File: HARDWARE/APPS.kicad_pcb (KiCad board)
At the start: 2 copper layers, 100 x 75 mm, 69 parts, among them J4 Sygnały, J5 Diagnostyka, J8 Zasilanie+CAN, K1 FINDER-30.22, Q1 BSS138, SW1 SW_Push, U1 STM32L4P5RET6, U3 LM1117-3.3, U4 LM1117-3.3, U5 LM1117-3.3, U6 MCP2562-H-SN, U7 MCP6001-OT, U8 MCP6001-OT, Y1 Crystal_GND24

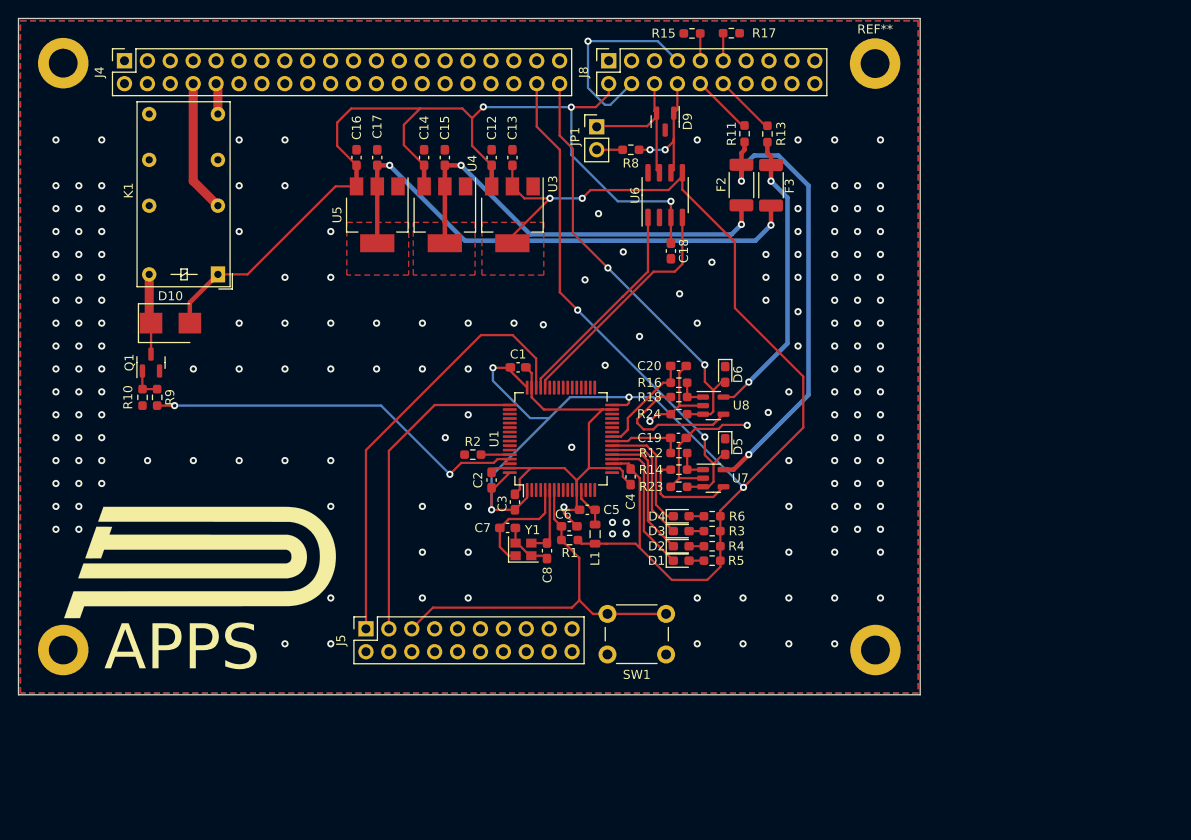
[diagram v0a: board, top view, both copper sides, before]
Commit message: Align components on the PCB
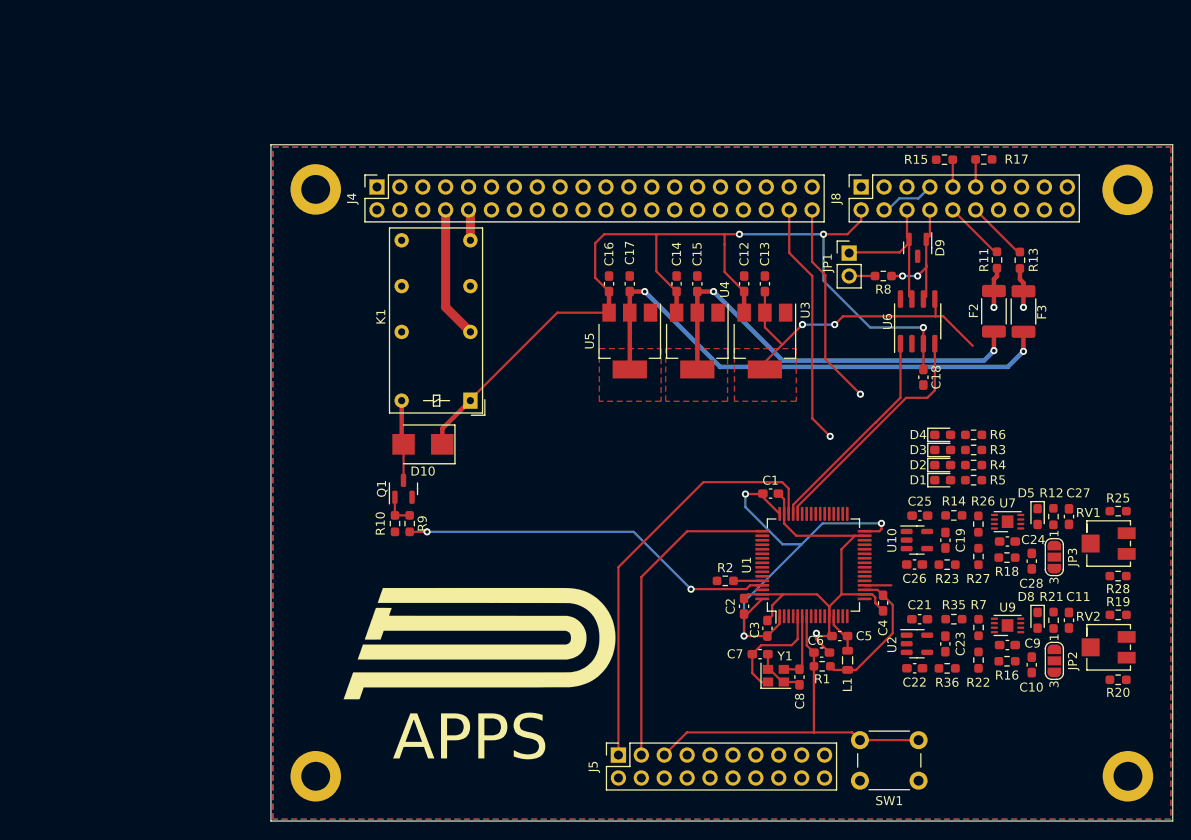
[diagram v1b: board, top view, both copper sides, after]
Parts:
- removed C20: 100n, Capacitor_SMD:C_0603_1608Metric_Pad1.08x0.95mm_HandSolder
- removed D6: D_TVS, Diode_SMD:D_0603_1608Metric_Pad1.05x0.95mm_HandSolder
- removed R24: 100k, Resistor_SMD:R_0603_1608Metric_Pad0.98x0.95mm_HandSolder
- removed U8: MCP6001-OT, Package_TO_SOT_SMD:SOT-23-5
- added C10: 10n, Capacitor_SMD:C_0603_1608Metric_Pad1.08x0.95mm_HandSolder, F.Cu at (184.4, 124.3)
- added C11: 10n, Capacitor_SMD:C_0603_1608Metric_Pad1.08x0.95mm_HandSolder, F.Cu at (188.5, 119.3)
- added C21: 100n, Capacitor_SMD:C_0603_1608Metric_Pad1.08x0.95mm_HandSolder, F.Cu at (172.0, 119.2)
- added C22: 100n, Capacitor_SMD:C_0603_1608Metric_Pad1.08x0.95mm_HandSolder, F.Cu at (171.4, 124.6)
- added C23: 100n, Capacitor_SMD:C_0603_1608Metric_Pad1.08x0.95mm_HandSolder, F.Cu at (174.8, 121.9)
- added C24: 100n, Capacitor_SMD:C_0603_1608Metric_Pad1.08x0.95mm_HandSolder, F.Cu at (181.7, 110.6)
- added C25: 100n, Capacitor_SMD:C_0603_1608Metric_Pad1.08x0.95mm_HandSolder, F.Cu at (172.0, 107.7)
- added C26: 100n, Capacitor_SMD:C_0603_1608Metric_Pad1.08x0.95mm_HandSolder, F.Cu at (171.4, 113.1)
- added C27: 10n, Capacitor_SMD:C_0603_1608Metric_Pad1.08x0.95mm_HandSolder, F.Cu at (188.5, 107.8)
- added C28: 10n, Capacitor_SMD:C_0603_1608Metric_Pad1.08x0.95mm_HandSolder, F.Cu at (184.4, 112.8)
- added C9: 100n, Capacitor_SMD:C_0603_1608Metric_Pad1.08x0.95mm_HandSolder, F.Cu at (181.7, 122.1)
- added D8: D_TVS, Diode_SMD:D_0603_1608Metric_Pad1.05x0.95mm_HandSolder, F.Cu at (185.1, 119.3)
- added JP2: POT/DAC, Jumper:SolderJumper-3_P1.3mm_Open_RoundedPad1.0x1.5mm_NumberLabels, F.Cu at (186.9, 123.8)
- added JP3: POT/DAC, Jumper:SolderJumper-3_P1.3mm_Open_RoundedPad1.0x1.5mm_NumberLabels, F.Cu at (186.9, 112.3)
- added R19: 10k, Resistor_SMD:R_0603_1608Metric_Pad0.98x0.95mm_HandSolder, F.Cu at (194.0, 118.7)
- added R20: 33k, Resistor_SMD:R_0603_1608Metric_Pad0.98x0.95mm_HandSolder, F.Cu at (194.0, 125.9)
- added R21: 100k, Resistor_SMD:R_0603_1608Metric_Pad0.98x0.95mm_HandSolder, F.Cu at (186.8, 119.3)
- added R22: TBD, Resistor_SMD:R_0603_1608Metric_Pad0.98x0.95mm_HandSolder, F.Cu at (178.5, 123.7)
- added R25: 10k, Resistor_SMD:R_0603_1608Metric_Pad0.98x0.95mm_HandSolder, F.Cu at (194.0, 107.2)
- added R26: TBD, Resistor_SMD:R_0603_1608Metric_Pad0.98x0.95mm_HandSolder, F.Cu at (178.5, 108.6)
- added R27: TBD, Resistor_SMD:R_0603_1608Metric_Pad0.98x0.95mm_HandSolder, F.Cu at (178.5, 112.2)
- added R28: 33k, Resistor_SMD:R_0603_1608Metric_Pad0.98x0.95mm_HandSolder, F.Cu at (194.0, 114.4)
- added R35: 4k7, Resistor_SMD:R_0603_1608Metric_Pad0.98x0.95mm_HandSolder, F.Cu at (175.8, 119.2)
- added R36: 4k7, Resistor_SMD:R_0603_1608Metric_Pad0.98x0.95mm_HandSolder, F.Cu at (175.0, 124.6)
- added R7: TBD, Resistor_SMD:R_0603_1608Metric_Pad0.98x0.95mm_HandSolder, F.Cu at (178.5, 120.1)
- added RV1: 1k, Potentiometer_SMD:Potentiometer_Bourns_3214J_Horizontal, F.Cu at (192.9, 110.8)
- added RV2: 1k, Potentiometer_SMD:Potentiometer_Bourns_3214J_Horizontal, F.Cu at (192.9, 122.3)
- added U10: MCP6001, Package_TO_SOT_SMD:SOT-23-5, F.Cu at (171.7, 110.4)
- added U2: MCP6001, Package_TO_SOT_SMD:SOT-23-5, F.Cu at (171.7, 121.9)
- added U9: MCP6N11-005, Package_DFN_QFN:TDFN-8-1EP_3x2mm_P0.5mm_EP1.3x1.4mm, F.Cu at (181.7, 119.9)
- R12: value 4k7 -> 100k
- R14: value 0R -> 4k7
- R16: value 4k7 -> 0R
- R23: value 100k -> 4k7
- U7: value MCP6001-OT -> MCP6N11-005; footprint Package_TO_SOT_SMD:SOT-23-5 -> Package_DFN_QFN:TDFN-8-1EP_3x2mm_P0.5mm_EP1.3x1.4mm
- moved R16 47.7 mm to (181.7, 123.9)
- moved R12 42.1 mm to (186.8, 107.8), turned to 90 degrees
- moved R18 40.5 mm to (181.7, 112.4), turned to 0 degrees
- moved D5 35.5 mm to (185.1, 107.8)
- moved U7 33.0 mm to (181.7, 108.4), turned to 180 degrees
- moved G*** 32.3 mm to (122.3, 121.6)
- moved C19 31.7 mm to (174.8, 110.4), turned to -90 degrees
- moved C13 31.3 mm to (154.8, 82.0)
- moved C16 31.3 mm to (137.5, 82.0)
- moved U3 31.3 mm to (154.8, 88.3)
- moved J5 31.3 mm to (138.6, 134.3)
- moved ? 31.3 mm to (195.0, 71.6)
- moved ? 31.3 mm to (195.1, 136.6)
- moved ? 31.3 mm to (105.0, 136.6)
- moved C1 31.3 mm to (155.5, 105.3)
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- renumbered REF** to ?
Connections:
- net /CAN-RX renamed /CAN_RX
- net /CAN-TX renamed /CAN_TX
- net /PowerModule/VO_POT1 renamed /Power Module/VO_POT1
- net /PowerModule/VO_POT2 renamed /Power Module/VO_POT2
- C19 pad 1: /SENSOR1 -> Net-(C19-Pad1)
- C19 pad 2: GND -> /SENSOR2
- D10 pad 1: Net-(D10-Pad1) -> +5V
- D10 pad 2: +5V -> Net-(D10-A)
- D5 pad 2: SIG_APPS1 -> SIG_APPS2
- K1 pad A2: Net-(D10-Pad1) -> Net-(D10-A)
- Q1 pad 3: Net-(D10-Pad1) -> Net-(D10-A)
- R12 pad 1: /SENSOR1 -> SIG_APPS2
- R12 pad 2: Net-(R12-Pad2) -> GND
- R14 pad 1: Net-(R12-Pad2) -> Net-(R14-Pad1)
- R14 pad 2: Net-(R14-Pad2) -> Net-(C19-Pad1)
- R16 pad 1: /SENSOR2 -> Net-(U9-EN)
- R16 pad 2: Net-(R16-Pad2) -> 3V3_POT1
- R18 pad 1: Net-(R16-Pad2) -> Net-(U7-EN)
- R18 pad 2: Net-(R18-Pad2) -> 3V3_POT2
- R23 pad 1: SIG_APPS1 -> Net-(C19-Pad1)
- R23 pad 2: GND -> Net-(U10-+)
- U1 pad 20: /LED1 -> /DAC_REF1
- U1 pad 21: /LED2 -> /DAC_REF2
- U1 pad 22: /LED3 -> unconnected-(U1-PA6-Pad22)
- U1 pad 23: /LED4 -> unconnected-(U1-PA7-Pad23)
- U1 pad 26: unconnected-(U1-Pad26) -> /LED1
- U1 pad 27: unconnected-(U1-Pad27) -> /LED2
- U1 pad 28: unconnected-(U1-Pad28) -> /LED3
- U1 pad 29: unconnected-(U1-Pad29) -> /LED4
- U7 pad 1: Net-(R12-Pad2) -> Net-(U7-FG)
- U7 pad 2: GND -> Net-(JP3-C)
- U7 pad 3: SIG_APPS1 -> SIG_APPS2
- U7 pad 4: Net-(R14-Pad2) -> GND
- U7 pad 5: 3V3_POT1 -> GND
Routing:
- net /3V3_SYS: track 179.9 -> 101.9 mm, vias 6 -> 5
- net 3V3_POT1: track 51.4 -> 4.44 mm, vias 2 -> 1
- net GND: track 106.3 -> 62.3 mm, vias 182 -> 1
- net SIG_APPS1: track 57.2 -> 27.0 mm, vias 2 -> 1
- net 3V3_POT2: track 32.8 -> 4.47 mm, vias 2 -> 1
- net SIG_APPS2: track 48.1 -> 22.7 mm, vias 2 -> 1
- net /LED1: track 15.8 -> 0.00 mm
- net Net-(R18-Pad2): track 15.7 -> 0.00 mm
- net /LED2: track 14.9 -> 0.00 mm
- net /LED3: track 13.9 -> 0.00 mm
- net /LED4: track 13.3 -> 0.00 mm
- net /SENSOR2: track 11.6 -> 0.00 mm
- net Net-(R14-Pad2): track 11.3 -> 0.00 mm
- net Net-(D10-Pad1): track 8.93 -> 0.00 mm
- net Net-(D10-A): track 0.00 -> 8.93 mm
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
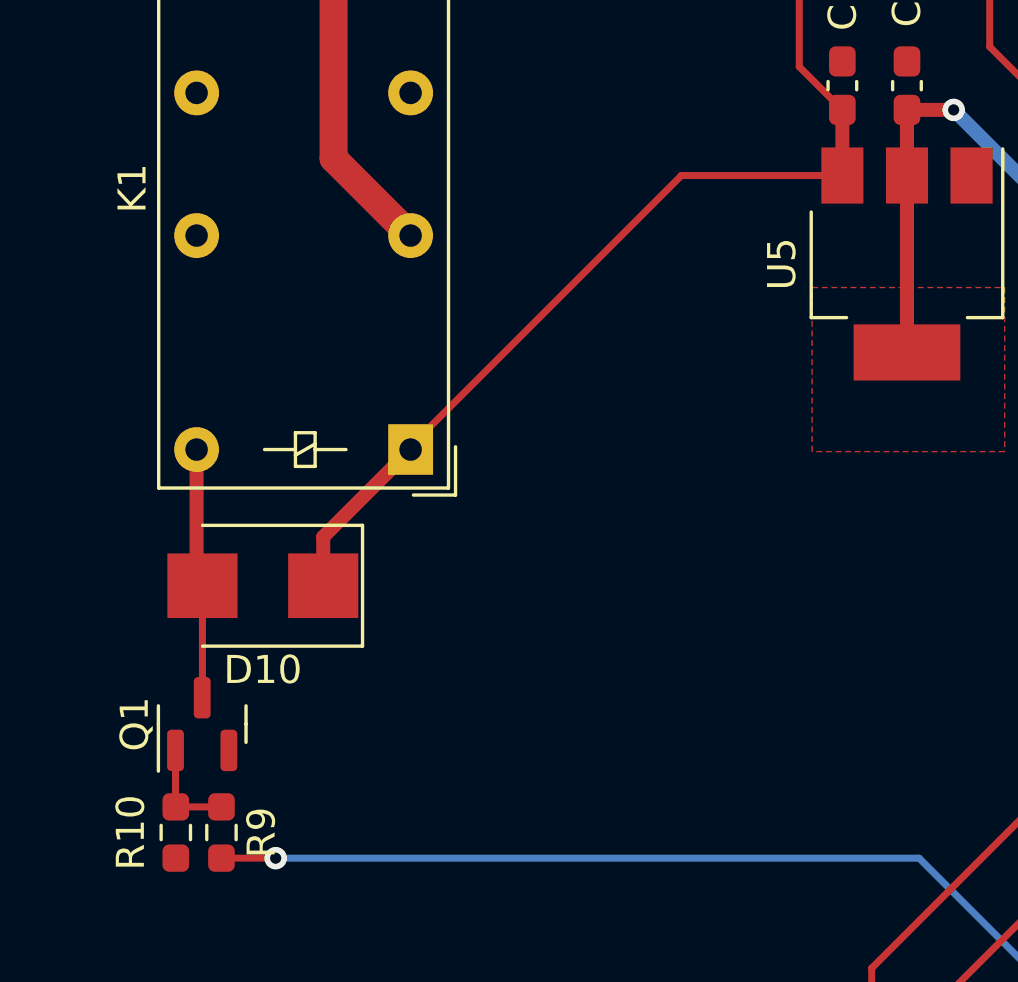
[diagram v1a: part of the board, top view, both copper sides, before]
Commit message: KiCad project refactor
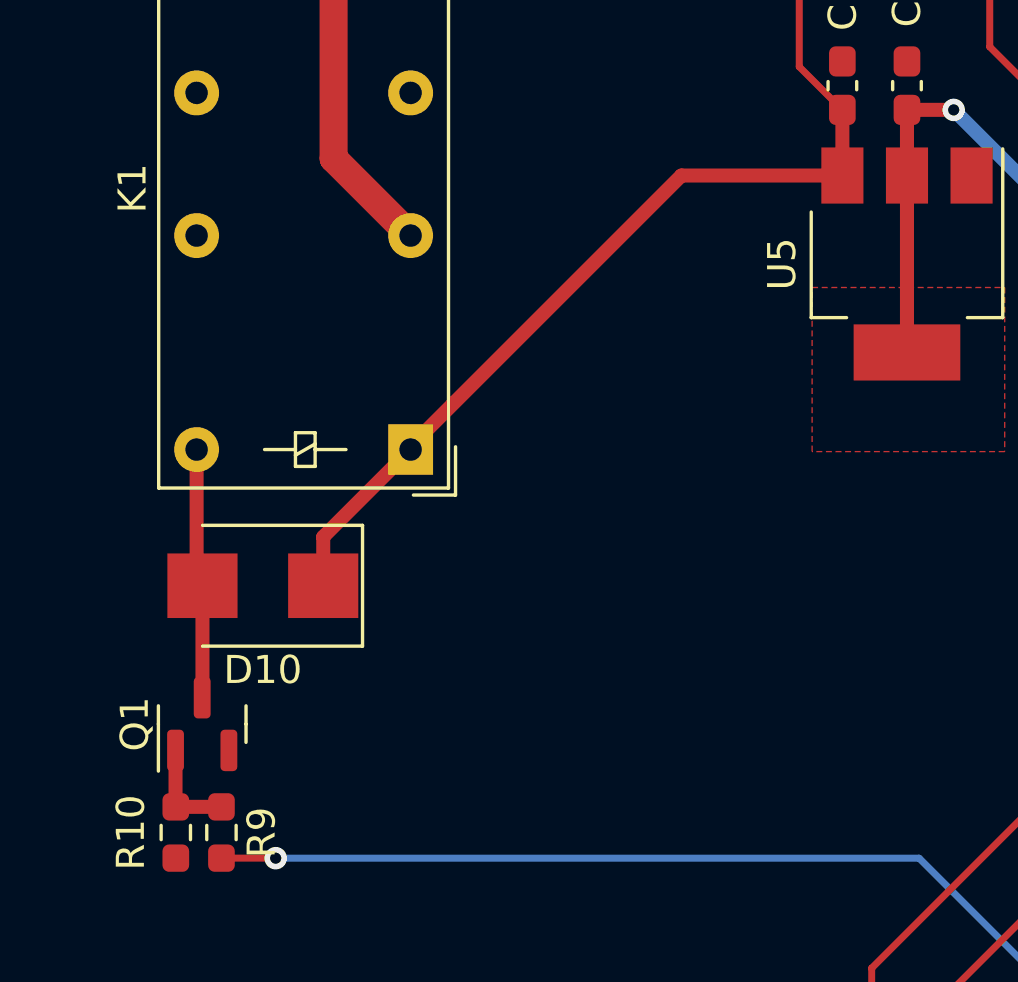
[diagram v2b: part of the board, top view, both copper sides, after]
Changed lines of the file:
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@@
     (effects (font (size 5 5) (thickness 1)))
-  )
-  (dimension (type aligned) (layer "Dwgs.User")
-    (pts (xy 72.046008 52.573201) (xy 172.046008 52.573201))
-    (height -8.373201)
-    (gr_text "100.0000 mm" (at 122.046008 43.05) (layer "Dwgs.User")
-      (effects (font (size 1 1) (thickness 0.15)))
-    )
-    (format (prefix "") (suffix "") (units 3) (units_format 1) (precision 4))
-    (style (thickness 0.1) (arrow_length 1.27) (text_position_mode 0) (extension_height 0.58642) (extension_offset 0.5) keep_text_aligned)
   )
   (segment (start 167.065 116.779994) (end 166.722006 116.437) (width 0.25) (layer "F.Cu") (net 1))
@@
   (segment (start 172.399 86.846907) (end 172.399 88.6364) (width 0.25) (layer "F.Cu") (net 5))
   (segment (start 136 77.5008) (end 136 81.3221) (width 0.25) (layer "F.Cu") (net 5))
-  (segment (start 122.1615 94.8385) (end 131.8042 85.1958) (width 0.25) (layer "F.Cu") (net 5))
+  (segment (start 122.1615 94.8385) (end 131.8042 85.1958) (width 0.5) (layer "F.Cu") (net 5))
   (segment (start 161.32 76.5) (end 163.9756 76.5) (width 0.25) (layer "F.Cu") (net 5))
   (segment (start 150.3518 77.627) (end 150.3518 80.6879) (width 0.25) (layer "F.Cu") (net 5))
-  (segment (start 131.8042 85.1958) (end 137.5362 85.1958) (width 0.25) (layer "F.Cu") (net 5))
+  (segment (start 131.8042 85.1958) (end 137.5362 85.1958) (width 0.5) (layer "F.Cu") (net 5))
   (segment (start 142.7826 76.5928) (end 142.7826 80.6117) (width 0.25) (layer "F.Cu") (net 5))
   (segment (start 136 81.3221) (end 137.5362 82.8583) (width 0.25) (layer "F.Cu") (net 5))
@@
   (segment (start 152.5222 82.8583) (end 152.5222 85.1958) (width 0.5) (layer "F.Cu") (net 5))
   (segment (start 150.3332 76.5) (end 137.0008 76.5) (width 0.25) (layer "F.Cu") (net 5))
-  (segment (start 122.1615 94.9535) (end 122.1615 94.8385) (width 0.25) (layer "F.Cu") (net 5))
+  (segment (start 122.1615 94.9535) (end 122.1615 94.8385) (width 0.5) (layer "F.Cu") (net 5))
   (segment (start 137.0008 76.5) (end 136 77.5008) (width 0.25) (layer "F.Cu") (net 5))
   (segment (start 172.399 91.4965) (end 172.399 88.6364) (width 0.25) (layer "F.Cu") (net 5))
@@
   (segment (start 175.6502 68.229) (end 175.66 68.2388) (width 0.25) (layer "F.Cu") (net 105))
   (segment (start 175.66 68.2388) (end 175.66 71.26) (width 0.25) (layer "F.Cu") (net 105))
-  (segment (start 115.4268 107.6771) (end 113.8012 107.6771) (width 0.25) (layer "F.Cu") (net 110))
+  (segment (start 115.4268 107.6771) (end 113.8012 107.6771) (width 0.5) (layer "F.Cu") (net 110))
   (segment (start 113.791 107.6669) (end 113.8012 107.6771) (width 0.25) (layer "F.Cu") (net 110))
-  (segment (start 113.791 105.6663) (end 113.791 107.6669) (width 0.25) (layer "F.Cu") (net 110))
+  (segment (start 113.791 105.6663) (end 113.791 107.6669) (width 0.5) (layer "F.Cu") (net 110))
   (segment (start 151.3405 114.9396) (end 151.343101 114.936999) (width 0.25) (layer "F.Cu") (net 111))
   (segment (start 151.343101 114.936999) (end 154.5809 114.936999) (width 0.25) (layer "F.Cu") (net 111))
@@
   (segment (start 181.7716 91.216) (end 183.4988 89.4888) (width 0.5) (layer "B.Cu") (net 116))
   (segment (start 149.8566 91.216) (end 181.7716 91.216) (width 0.5) (layer "B.Cu") (net 116))
-  (segment (start 114.75 99.8025) (end 114.75 103.7823) (width 0.25) (layer "F.Cu") (net 117))
+  (segment (start 114.75 99.8025) (end 114.75 103.7823) (width 0.5) (layer "F.Cu") (net 117))
   (segment (start 114.5415 94.9535) (end 114.5415 99.594) (width 0.5) (layer "F.Cu") (net 117))
   (segment (start 114.5415 99.594) (end 114.75 99.8025) (width 0.5) (layer "F.Cu") (net 117))
